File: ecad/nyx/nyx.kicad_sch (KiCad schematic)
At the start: 66 parts, among them J1 JST XH, J2 JST PH, J3 JST SH, Q1 RD3P01BAT, Q2 NMBTA56, Q3 DMPH6250S, U1 THVD8010, U3 ATtiny202-SS, U4 LMR36500P3RPE, U5 TPS92512

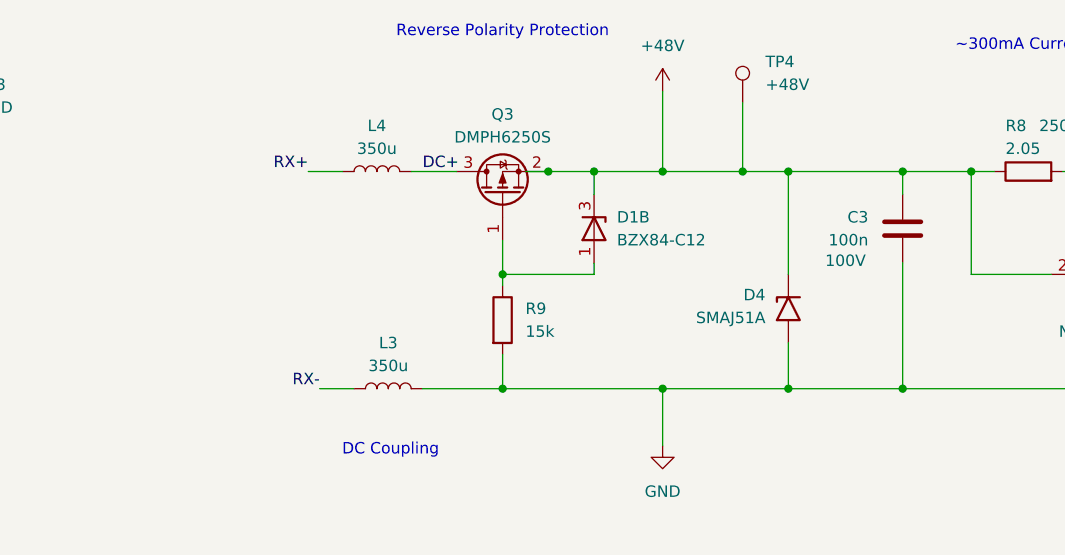
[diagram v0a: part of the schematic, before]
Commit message: Updates nyx to block reverse current
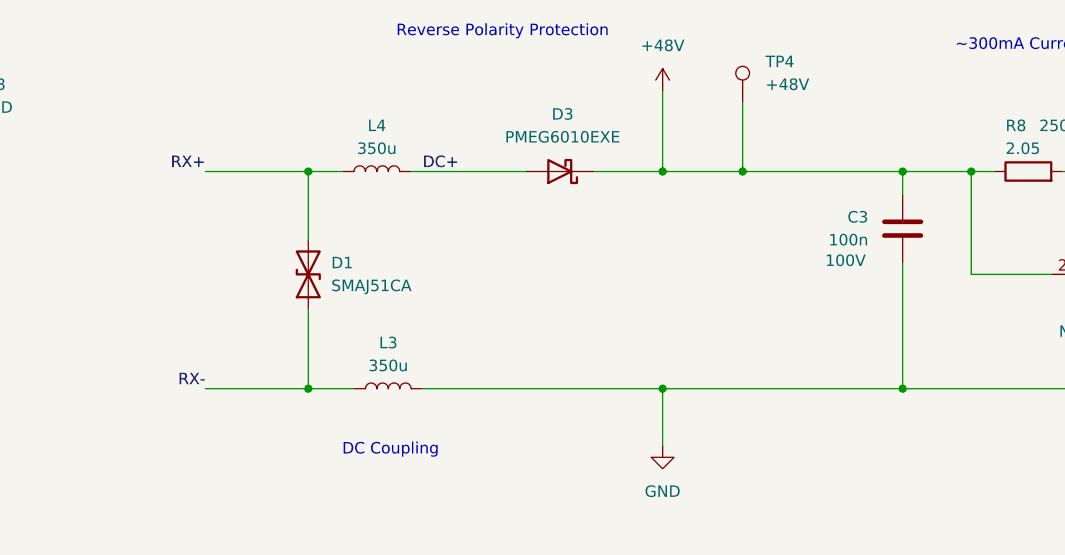
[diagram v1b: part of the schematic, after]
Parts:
- removed D1: BZX84-C12, Package_TO_SOT_SMD:SOT-23, symbol Device:D_Zener_Dual_CommonAnode_AKK_Split
- removed D4: SMAJ51A, Diode_SMD:D_SMA, symbol Diode:SMAJ58A
- removed Q3: DMPH6250S, Package_TO_SOT_SMD:SOT-23, symbol Device:Q_PMOS_GSD
- removed R9: 15k, Resistor_SMD:R_0402_1005Metric, symbol Device:R
- added D1: SMAJ51CA, Diode_SMD:D_SMA, symbol Device:D_TVS
- added D3: PMEG6010EXE, fort:Nexperia_CFP3-HP_SOD-123HP, symbol Device:D_Schottky
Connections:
- net +48V: now also D3.1 (K)
- net DC+: now also D3.2 (A)
- net RX+: now also D1.2 (A2)
- net RX-: now also D1.1 (A1)

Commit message: Updates MPN for new PCBs
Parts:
- C1, C9: MPN (none) -> C1206F184K1RACAUTO
- C10, C12, C13, C18, C19, C21: MPN (none) -> CL32Y475MCIVPNE
- C11, C15, C17, C2, C22, C7: MPN (none) -> GRM155R71H104KE14J
- C16, C20, C3, C4: MPN (none) -> CL10B104KC8NNNC
- C5: MPN (none) -> CL32B225KCJSNNE
- C6: MPN (none) -> CL10B105MO8NNWC
- C8: value 3.3u -> 10u; MPN (none) -> GRM21BR71A106MA73L
- J2: MPN (none) -> B4B-PH-SM4-TB
- J3: MPN (none) -> BM03B-SRSS-TB
- Q1: MPN (none) -> RD3P01BAT
- Q2: MPN (none) -> NMBTA56
- R1, R10, R18, R5: MPN (none) -> RC0402FR-0715KL
- R11: MPN (none) -> RC0402FR-0710ML
- R12: MPN (none) -> RC0402FR-07270KL
- R13: MPN (none) -> RC0402FR-07300KL
- R14: MPN (none) -> RC0402FR-078K2L
- R15, R16: MPN (none) -> KDV12DR300ET
- R17: MPN (none) -> RC0402FR-071KL
- R19: MPN (none) -> RK73B2ATTD333J
- R2: MPN (none) -> RC0402FR-0747KL
- R3: MPN (none) -> ERJ-2RKF1200X
- R4: MPN (none) -> RC0402FR-07560KL
- R6: MPN (none) -> RC0402FR-0733KL
- R7: MPN (none) -> RC0402FR-0768KL
- R8: MPN (none) -> RC1206FR-072R05L
- TP1: value RX+ -> 5019
- TP2: value RX- -> 5019
- TP3: value GND -> 5019
- TP4: value +48V -> 5019
- TP5: value VIN -> 5019
- TP6, TP7: value RX -> 5019
- U1: MPN (none) -> THVD8010
- U3: MPN (none) -> ATtiny202-SS
- U4: MPN (none) -> LMR36500P3RPE
- U5: value TPS92512 -> TPS92512HV; MPN (none) -> TPS92512HV

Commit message: upload to pcbway
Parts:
- Q2: value NMBTA56 -> MMBTA56
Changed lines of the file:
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@@
 			)
 		)
-		(property "Value" "NMBTA56"
+		(property "Value" "MMBTA56"
 			(at 182.88 54.61 90)
 			(effects

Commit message: [NYX] Updates wrong UVLO resistance value
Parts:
- D5: value 100V,3A -> SK3BA
- R4: value 560k -> 510k
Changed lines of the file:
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@@
 (kicad_sch
-	(version 20231120)
+	(version 20250114)
 	(generator "eeschema")
-	(generator_version "8.0")
+	(generator_version "9.0")
 	(paper "A3")
+	(text "Reverse Polarity Protection"
+		(exclude_from_sim no)
+		(at 116.84 21.336 0)
+		(effects
+			(font
+				(size 1.27 1.27)
+			)
+		)
+	)
+	(text "AC Coupling"
+		(exclude_from_sim no)
+		(at 47.244 113.538 0)
+		(effects
+			(font
+				(size 1.27 1.27)
+			)
+		)
+	)
+	(text "DC Coupling"
+		(exclude_from_sim no)
+		(at 104.394 67.818 0)
+		(effects
+			(font
+				(size 1.27 1.27)
+			)
+		)
+	)
+	(text "~300mA Current Limiter with 700mV Dropout"
+		(exclude_from_sim no)
+		(at 187.198 22.86 0)
+		(effects
+			(font
+				(size 1.27 1.27)
+			)
+		)
+	)
 	(junction
 		(at 212.09 36.83)
@@
 		)
 	)
-	(text "Reverse Polarity Protection"
-		(exclude_from_sim no)
-		(at 116.84 21.336 0)
-		(effects
-			(font
-				(size 1.27 1.27)
-			)
-		)
-	)
-	(text "AC Coupling"
-		(exclude_from_sim no)
-		(at 47.244 113.538 0)
-		(effects
-			(font
-				(size 1.27 1.27)
-			)
-		)
-	)
-	(text "DC Coupling"
-		(exclude_from_sim no)
-		(at 104.394 67.818 0)
-		(effects
-			(font
-				(size 1.27 1.27)
-			)
-		)
-	)
-	(text "~300mA Current Limiter with 700mV Dropout"
-		(exclude_from_sim no)
-		(at 187.198 22.86 0)
-		(effects
-			(font
-				(size 1.27 1.27)
-			)
-		)
-	)
 	(label "IR_ON"
 		(at 220.98 201.93 0)
-		(fields_autoplaced yes)
 		(effects
 			(font
@@
 	(label "LED_BOOT"
 		(at 283.21 106.68 90)
-		(fields_autoplaced yes)
 		(effects
 			(font
@@
 	(label "RG_VCC"
 		(at 323.85 49.53 180)
-		(fields_autoplaced yes)
 		(effects
 			(font
@@
 	(label "DC+"
 		(at 107.95 36.83 0)
-		(fields_autoplaced yes)
 		(effects
 			(font
@@
 	(label "IR_ON"
 		(at 250.19 115.57 180)
-		(fields_autoplaced yes)
 		(effects
 			(font
@@
 	(label "RX_DCP+"
 		(at 60.96 133.35 0)
-		(fields_autoplaced yes)
 		(effects
 			(font
@@
 	(label "LED_UVLO"
 		(at 243.84 123.19 0)
-		(fields_autoplaced yes)
 		(effects
 			(font
@@
 	(label "RX+"
 		(at 38.1 133.35 180)
-		(fields_autoplaced yes)
 		(effects
 			(font
@@
 	(label "LED_SW"
 		(at 284.48 111.76 0)
-		(fields_autoplaced yes)
 		(effects
 			(font
@@
 	(label "RX_DCP-"
 		(at 60.96 156.21 0)
-		(fields_autoplaced yes)
 		(effects
 			(font
@@
 	(label "LED_SENSE_PRT"
 		(at 281.94 120.65 0)
-		(fields_autoplaced yes)
 		(effects
 			(font
@@
 	(label "I_LIM_G"
 		(at 201.93 49.53 0)
-		(fields_autoplaced yes)
 		(effects
 			(font
@@
 	(label "UDPI{slash}~{RST}"
 		(at 209.55 196.85 0)
-		(fields_autoplaced yes)
 		(effects
 			(font
@@
 	(label "UDPI{slash}~{RST}"
 		(at 356.87 46.99 0)
-		(fields_autoplaced yes)
 		(effects
 			(font
@@
 	(label "UDPI{slash}~{RST}"
 		(at 266.7 190.5 180)
-		(fields_autoplaced yes)
 		(effects
 			(font
@@
 	(label "RG_UVLO"
 		(at 312.42 39.37 0)
-		(fields_autoplaced yes)
 		(effects
 			(font
@@
 	(label "RG_SW"
 		(at 347.98 39.37 0)
-		(fields_autoplaced yes)
 		(effects
 			(font
@@
 	(label "RX"
 		(at 204.47 209.55 0)
-		(fields_autoplaced yes)
 		(effects
 			(font
@@
 	(label "RX"
 		(at 120.65 144.78 0)
-		(fields_autoplaced yes)
 		(effects
 			(font
@@
 	(label "LED-"
 		(at 353.06 127 0)
-		(fields_autoplaced yes)
 		(effects
 			(font
@@
 	(label "RX-"
 		(at 83.82 60.96 180)
-		(fields_autoplaced yes)
 		(effects
 			(font
@@
 	(label "RG_BOOT"
 		(at 347.98 34.29 90)
-		(fields_autoplaced yes)
 		(effects
 			(font
@@
 	(label "LED_CMP"
 		(at 247.65 125.73 0)
-		(fields_autoplaced yes)
 		(effects
 			(font
@@
 	(label "I_IN_MS"
 		(at 185.42 36.83 0)
-		(fields_autoplaced yes)
 		(effects
 			(font
@@
 	(label "RX-"
 		(at 38.1 156.21 180)
-		(fields_autoplaced yes)
 		(effects
 			(font
@@
 	(label "LED+"
 		(at 353.06 111.76 0)
-		(fields_autoplaced yes)
 		(effects
 			(font
@@
 	(label "RX-"
 		(at 39.37 38.1 0)
-		(fields_autoplaced yes)
 		(effects
 			(font
@@
 	(label "RX+"
 		(at 39.37 35.56 0)
-		(fields_autoplaced yes)
 		(effects
 			(font
@@
 	(label "RG_FB"
 		(at 347.98 44.45 0)
-		(fields_autoplaced yes)
 		(effects
 			(font
@@
 	(label "RX+"
 		(at 83.82 36.83 180)
-		(fields_autoplaced yes)
 		(effects
 			(font
@@
 			)
 		)
-		(property "Value" "560k"
+		(property "Value" "510k"
 			(at 303.53 43.1799 0)
 			(effects
@@
 		(on_board yes)
 		(dnp no)
-		(fields_autoplaced yes)
 		(property "Reference" "D5"
 			(at 302.26 116.5224 90)
@@
 			)
 		)
-		(property "Value" "100V,3A"
+		(property "Value" "SK3BA"
 			(at 302.26 119.0624 90)
 			(effects
@@
 			)
 		)
-		(property "Description" "Schottky diode"
-			(at 299.72 118.11 0)
+		(property "Description" "100V, 3A"
+			(at 305.816 121.666 90)
 			(effects
 				(font
 					(size 1.27 1.27)
 				)
-				(hide yes)
 			)
 		)
@@
 		)
 	)
+	(embedded_fonts no)
 )

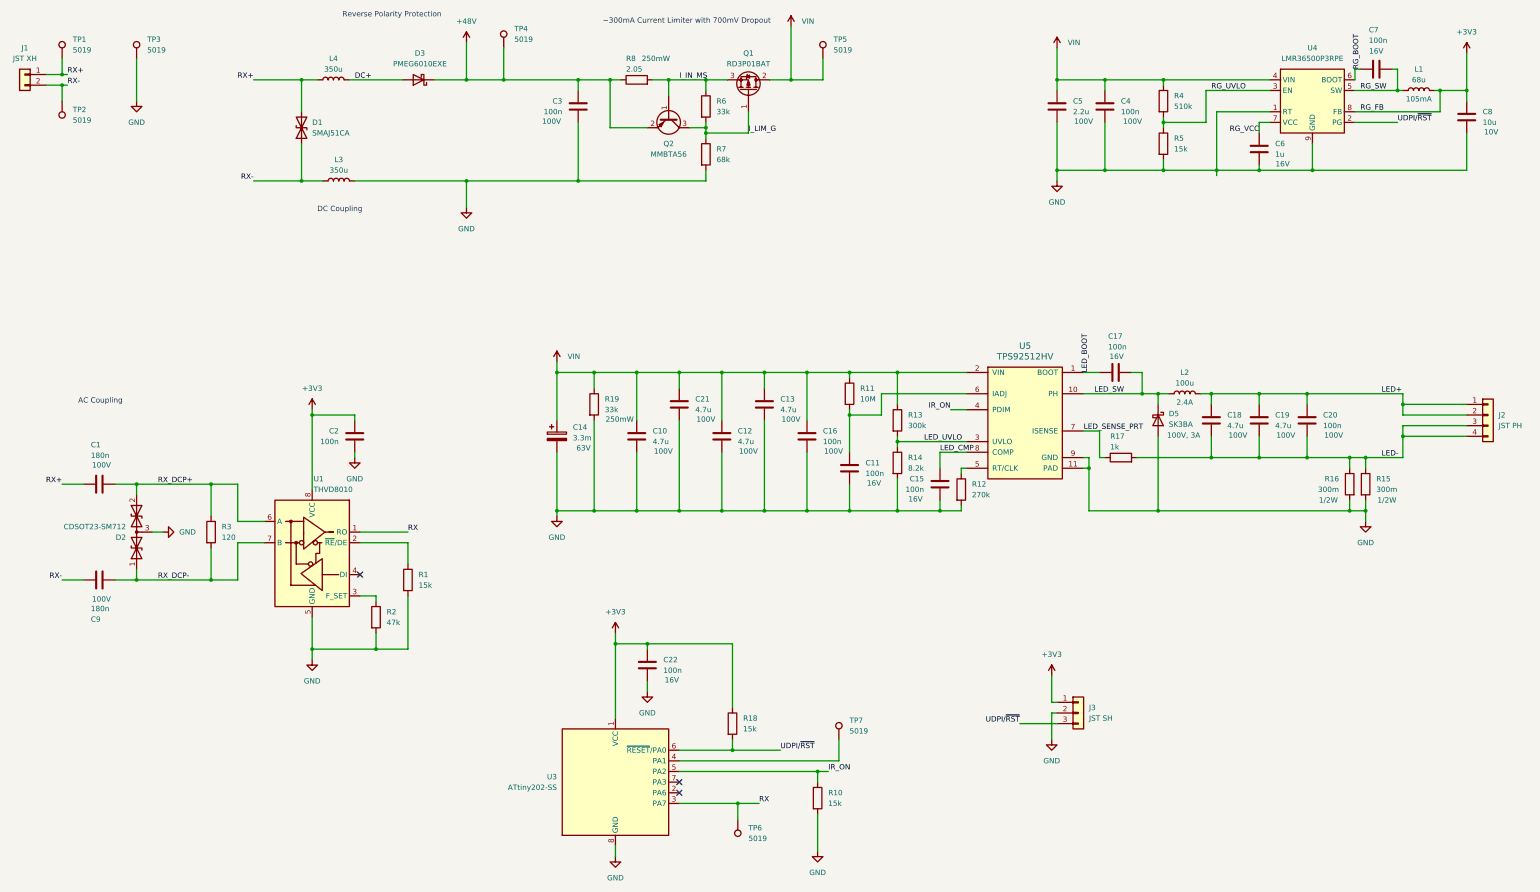
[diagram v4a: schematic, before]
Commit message: Updates nyx layout fore manufacturability.
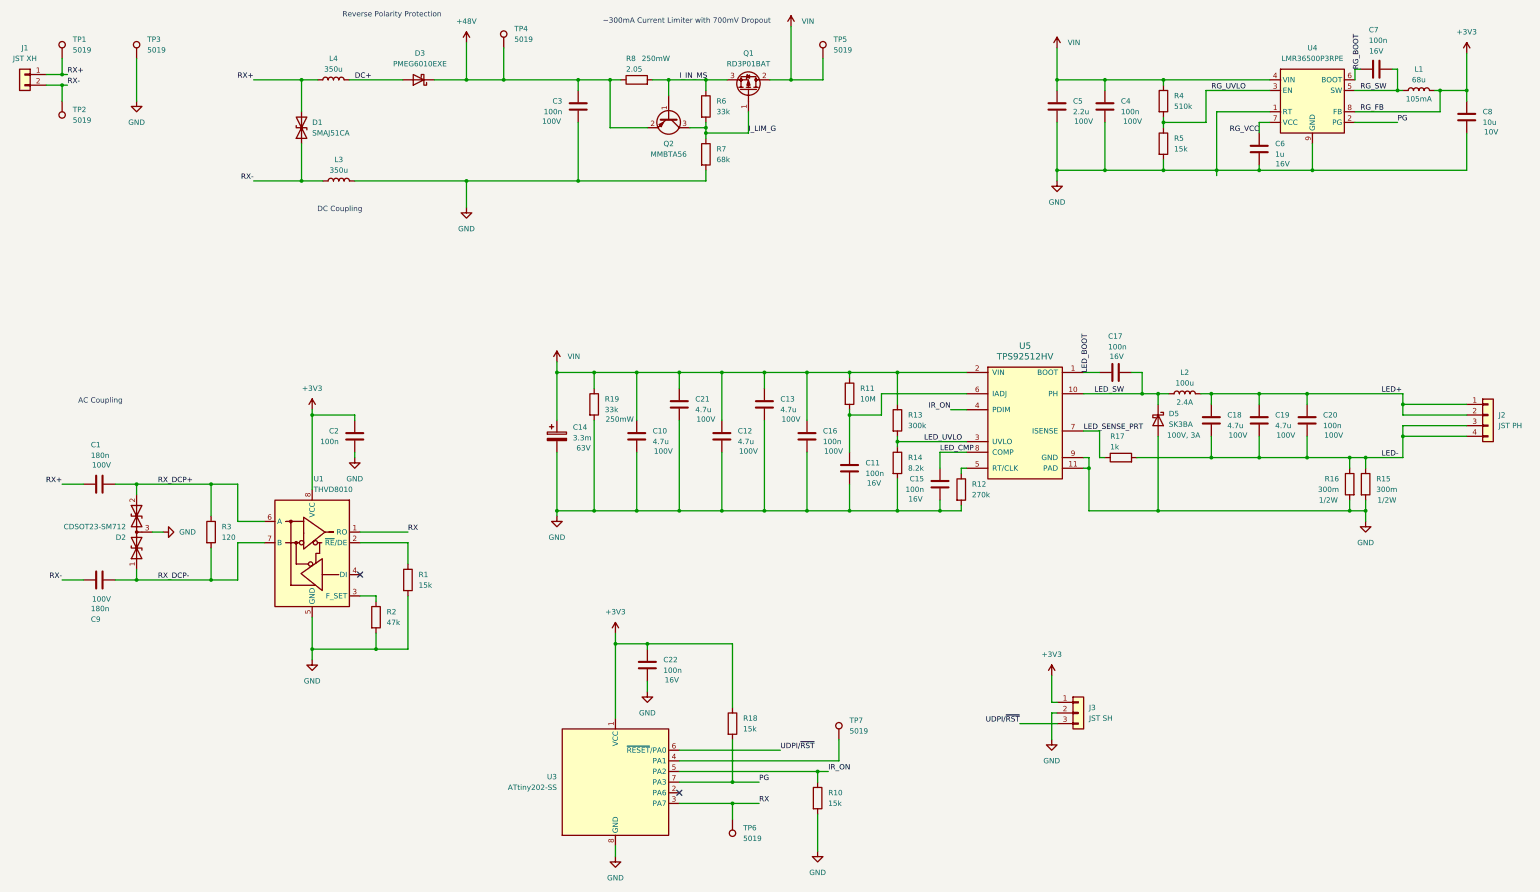
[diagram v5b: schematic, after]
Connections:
- net UDPI/~{RST}: no longer R18.2, U4.2 (PG)
- net PG: now reaches U3.7 (PA3)
- net PG: now also R18.2, U4.2 (PG)
- no-connect marks 3 -> 2
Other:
- moved on the sheet: TP6
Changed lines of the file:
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@@
 	)
 	(junction
+		(at 198.12 204.47)
+		(diameter 0)
+		(color 0 0 0 0)
+	)
+	(junction
 		(at 73.66 133.35)
 		(diameter 0)
@@
 	)
 	(junction
-		(at 199.39 209.55)
+		(at 198.12 209.55)
 		(diameter 0)
 		(color 0 0 0 0)
@@
 	)
 	(junction
-		(at 198.12 196.85)
-		(diameter 0)
-		(color 0 0 0 0)
-	)
-	(junction
 		(at 299.72 139.7)
 		(diameter 0)
@@
 	)
 	(no_connect
-		(at 185.42 204.47)
-	)
-	(no_connect
 		(at 185.42 207.01)
 	)
@@
 	(wire
 		(pts
+			(xy 198.12 204.47) (xy 204.47 204.47)
+		)
+		(stroke
+			(width 0)
+			(type default)
+		)
+	)
+	(wire
+		(pts
 			(xy 205.74 118.11) (xy 205.74 139.7)
 		)
@@
 	(wire
 		(pts
+			(xy 198.12 204.47) (xy 185.42 204.47)
+		)
+		(stroke
+			(width 0)
+			(type default)
+		)
+	)
+	(wire
+		(pts
 			(xy 195.58 139.7) (xy 185.42 139.7)
 		)
@@
 	(wire
 		(pts
-			(xy 198.12 196.85) (xy 209.55 196.85)
-		)
-		(stroke
-			(width 0)
-			(type default)
-		)
-	)
-	(wire
-		(pts
 			(xy 275.59 58.42) (xy 275.59 60.96)
 		)
@@
 	(wire
 		(pts
-			(xy 199.39 209.55) (xy 204.47 209.55)
+			(xy 198.12 209.55) (xy 204.47 209.55)
 		)
 		(stroke
@@
 	(wire
 		(pts
+			(xy 198.12 194.31) (xy 198.12 204.47)
+		)
+		(stroke
+			(width 0)
+			(type default)
+		)
+	)
+	(wire
+		(pts
 			(xy 326.39 46.99) (xy 323.85 46.99)
 		)
@@
 	(wire
 		(pts
-			(xy 199.39 209.55) (xy 199.39 213.36)
+			(xy 198.12 209.55) (xy 198.12 213.36)
 		)
 		(stroke
@@
 	(wire
 		(pts
-			(xy 198.12 194.31) (xy 198.12 196.85)
-		)
-		(stroke
-			(width 0)
-			(type default)
-		)
-	)
-	(wire
-		(pts
 			(xy 207.01 36.83) (xy 212.09 36.83)
 		)
@@
 	(wire
 		(pts
-			(xy 185.42 196.85) (xy 198.12 196.85)
+			(xy 185.42 196.85) (xy 209.55 196.85)
 		)
 		(stroke
@@
 	(wire
 		(pts
-			(xy 185.42 209.55) (xy 199.39 209.55)
+			(xy 185.42 209.55) (xy 198.12 209.55)
 		)
 		(stroke
@@
 		)
 	)
+	(label "PG"
+		(at 204.47 204.47 0)
+		(effects
+			(font
+				(size 1.27 1.27)
+			)
+			(justify left bottom)
+		)
+	)
 	(label "I_LIM_G"
 		(at 201.93 49.53 0)
@@
 		)
 	)
-	(label "UDPI{slash}~{RST}"
+	(label "PG"
 		(at 356.87 46.99 0)
 		(effects
@@
 	(symbol
 		(lib_id "Connector:TestPoint")
-		(at 199.39 213.36 180)
+		(at 198.12 213.36 180)
 		(unit 1)
 		(exclude_from_sim no)
@@
 		(fields_autoplaced yes)
 		(property "Reference" "TP6"
-			(at 201.93 215.3919 0)
+			(at 200.66 215.3919 0)
 			(effects
 				(font
@@
 		)
 		(property "Value" "5019"
-			(at 201.93 217.9319 0)
+			(at 200.66 217.9319 0)
 			(effects
 				(font
@@
 		)
 		(property "Footprint" "fort:TestPoint_Keystone_5019_Minature"
-			(at 194.31 213.36 0)
+			(at 193.04 213.36 0)
 			(effects
 				(font
@@
 		)
 		(property "Datasheet" "~"
-			(at 194.31 213.36 0)
+			(at 193.04 213.36 0)
 			(effects
 				(font
@@
 		)
 		(property "Description" "test point"
-			(at 199.39 213.36 0)
+			(at 198.12 213.36 0)
 			(effects
 				(font
@@
 		)
 		(property "MPN" "5019"
-			(at 199.39 213.36 0)
+			(at 198.12 213.36 0)
 			(effects
 				(font

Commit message: Uses soft terminal capacitor.
It may reduce the noise, it will reduce the risk of craking.
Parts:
- C10, C12, C13, C18, C19, C21: MPN CL32Y475MCIVPNE -> CL32B475KCVZW6E
- C16, C20, C3, C4: MPN CL10B104KC8NNNC -> GCJ188R72A104MA01D
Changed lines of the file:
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@@
 			)
 		)
-		(property "MPN" "CL32Y475MCIVPNE"
+		(property "MPN" "CL32B475KCVZW6E"
 			(at 175.26 121.92 0)
 			(effects
@@
 			)
 		)
-		(property "MPN" "CL10B104KC8NNNC"
+		(property "MPN" "GCJ188R72A104MA01D"
 			(at 161.29 43.18 0)
 			(effects
@@
 			)
 		)
-		(property "MPN" "CL32Y475MCIVPNE"
+		(property "MPN" "CL32B475KCVZW6E"
 			(at 185.42 114.3 0)
 			(effects
@@
 			)
 		)
-		(property "MPN" "CL10B104KC8NNNC"
+		(property "MPN" "GCJ188R72A104MA01D"
 			(at 335.28 118.11 0)
 			(effects
@@
 			)
 		)
-		(property "MPN" "CL10B104KC8NNNC"
+		(property "MPN" "GCJ188R72A104MA01D"
 			(at 287.02 43.18 0)
 			(effects
@@
 			)
 		)
-		(property "MPN" "CL32Y475MCIVPNE"
+		(property "MPN" "CL32B475KCVZW6E"
 			(at 312.42 118.11 0)
 			(effects
@@
 			)
 		)
-		(property "MPN" "CL32Y475MCIVPNE"
+		(property "MPN" "CL32B475KCVZW6E"
 			(at 195.58 121.92 0)
 			(effects
@@
 			)
 		)
-		(property "MPN" "CL10B104KC8NNNC"
+		(property "MPN" "GCJ188R72A104MA01D"
 			(at 215.9 121.92 0)
 			(effects
@@
 			)
 		)
-		(property "MPN" "CL32Y475MCIVPNE"
+		(property "MPN" "CL32B475KCVZW6E"
 			(at 323.85 118.11 0)
 			(effects
@@
 			)
 		)
-		(property "MPN" "CL32Y475MCIVPNE"
+		(property "MPN" "CL32B475KCVZW6E"
 			(at 205.74 114.3 0)
 			(effects

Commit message: Updates nyx's bom
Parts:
- removed R18: 15k, Resistor_SMD:R_0402_1005Metric, symbol Device:R
- L3, L4: value 350u -> 330u
- R13: value 300k -> 240k; MPN RC0402FR-07300KL -> RC0402FR-07240KL
- R14: value 8.2k -> 6.8k; MPN RC0402FR-078K2L -> RC0402FR-076K8L
- TP1, TP2, TP4, TP5, TP6, TP7: now not fitted
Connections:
- net PG: no longer U3.7 (PA3)
- net CLK: now reaches R12.1, U5.5 (RT/CLK)
- net A1: now reaches TP7.1, U3.4 (PA1)
- no-connect marks 2 -> 3
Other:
- moved on the sheet: R10

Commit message: Fixes Nyx UVLO for wrong reference
Please change MPN when changing value
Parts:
- R4: value 510k -> 560k
- R5: value 15k -> 33k; MPN RC0402FR-0715KL -> RC0402FR-0733KL
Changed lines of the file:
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@@
 			)
 		)
-		(property "Value" "510k"
+		(property "Value" "560k"
 			(at 303.53 43.1799 0)
 			(effects
@@
 			)
 		)
-		(property "Value" "15k"
+		(property "Value" "33k"
 			(at 303.53 53.3399 0)
 			(effects
@@
 			)
 		)
-		(property "MPN" "RC0402FR-0715KL"
+		(property "MPN" "RC0402FR-0733KL"
 			(at 300.99 52.07 0)
 			(effects
